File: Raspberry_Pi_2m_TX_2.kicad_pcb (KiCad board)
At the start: 2 copper layers, 66 x 56.5 mm, 32 parts, among them J3 RPi_GPIO, P1 3Sip100, P2 4Sip200, P3 2Sip200, P4 SMA, P5 CONN_01X02, Q1 BC817-40, U1 L4940V5 1.5A

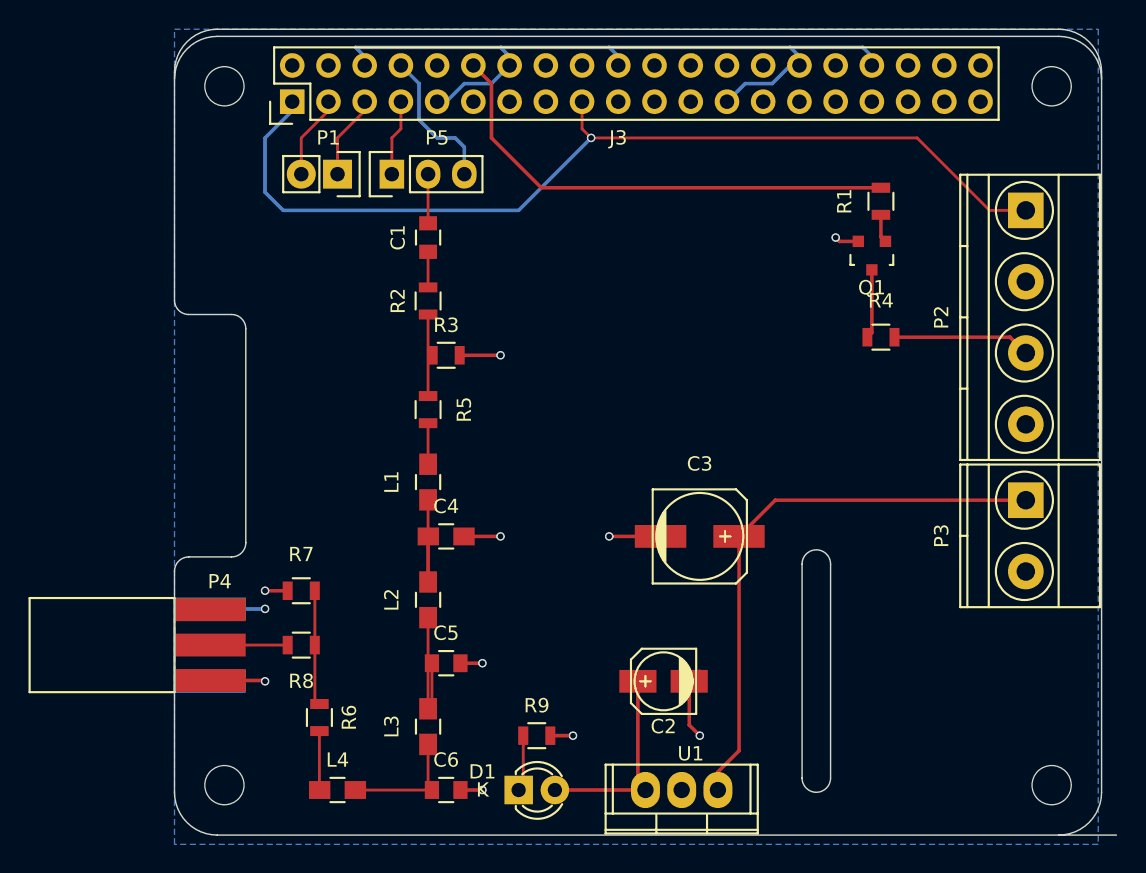
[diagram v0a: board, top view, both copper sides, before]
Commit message: Finished PCB but still need to do DRC
Almost complete
Still need to DRC and component check
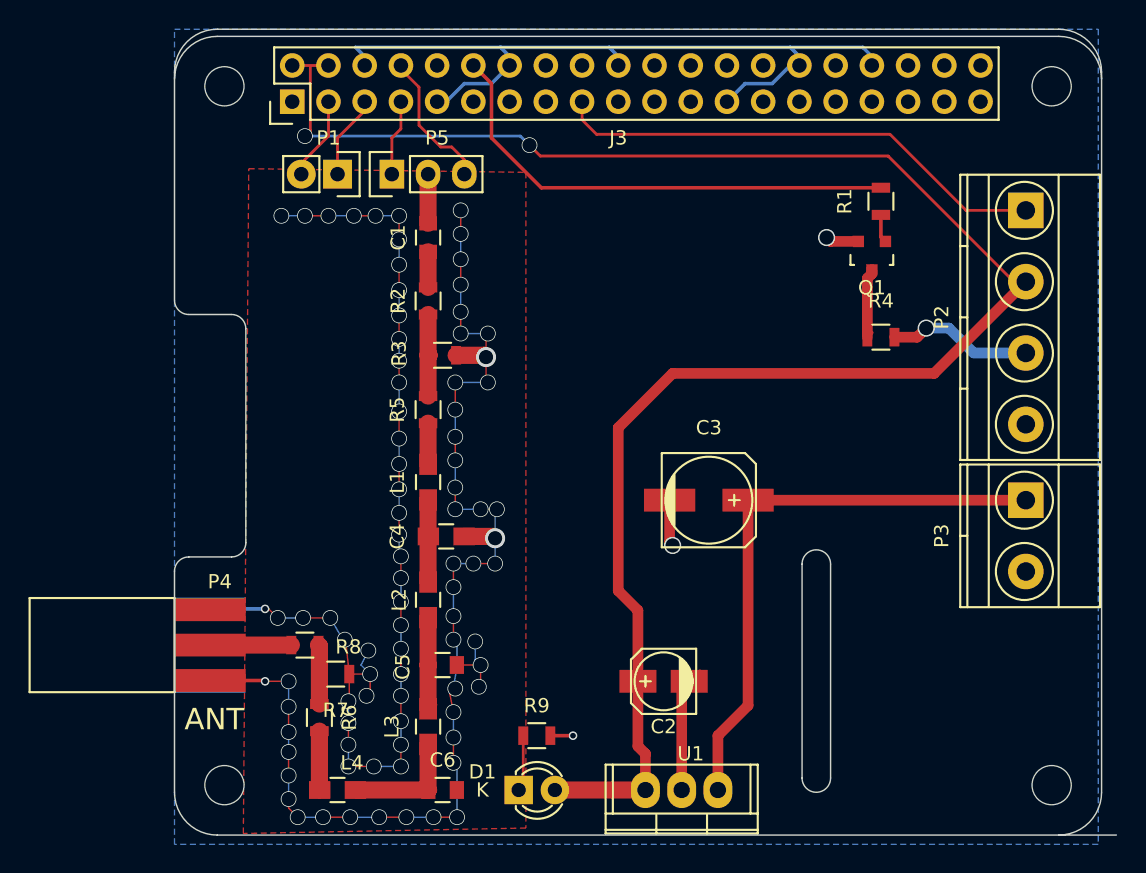
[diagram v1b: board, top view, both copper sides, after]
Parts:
- moved R7 6.32 mm to (46.9, 71.9), turned to 0 degrees
- moved C3 2.62 mm to (73.0, 59.7)
- moved C5 0.28 mm to (54.4, 71.2)
- moved C6 0.25 mm to (54.4, 80.0)
- moved R3 0.25 mm to (54.4, 49.5)
- moved R8 0.25 mm to (44.7, 69.8)
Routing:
- net GND: track 88.5 -> 239.1 mm, vias 11 -> 90
- net +5V: track 14.9 -> 129.2 mm, vias 0 -> 2
- net +3V3: track 68.0 -> 36.4 mm, vias 1 -> 0
- net Net-(R6-Pad1): track 8.07 -> 4.70 mm
- net Net-(C4-Pad1): track 8.96 -> 5.80 mm
- net Net-(C5-Pad1): track 9.70 -> 7.21 mm
- net Net-(C3-Pad1): track 39.6 -> 40.7 mm
- net Net-(J3-Pad3): track 5.87 -> 6.50 mm
- net Net-(P2-Pad3): track 9.67 -> 10.2 mm, vias 0 -> 1
- added copper zone on F.Cu, net GND
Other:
- net class +5V: trace_width 0.75 -> 1
- net class Default: trace_width 0.25 -> 1.2; via_dia 0.6 -> 1.1; via_drill 0.4 -> 1
- board text added: "ANT"

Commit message: Board is now compleate
Added second filter
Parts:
- added C7: 10nf, Capacitors_SMD:C_0805_HandSoldering, F.Cu at (48.8, 47.6)
- added F1: LFCN-80, Bacar:LFCN-80, F.Cu at (43.8, 40.6)
- added P6: CONN_01X02, Pin_Headers:Pin_Header_Straight_1x02, F.Cu at (48.8, 42.9)
- added P7: SMA, Bacar:SMA_Edge, F.Cu at (38.1, 40.8)
- added R10: oc, Resistors_SMD:R_0805_HandSoldering, F.Cu at (44.1, 50.5)
- added R11: 0, Resistors_SMD:R_0805_HandSoldering, F.Cu at (45.2, 45.7)
- added R12: 0, Resistors_SMD:R_0805_HandSoldering, F.Cu at (47.5, 53.8)
- moved D1 37.7 mm to (78.0, 47.0)
- moved R9 37.7 mm to (78.0, 42.5), turned to 90 degrees
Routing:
- net GND: track 239.1 -> 348.0 mm, vias 90 -> 138
- net +3V3: track 36.4 -> 57.9 mm
- net +5V: track 129.2 -> 109.5 mm
- net Net-(R10-Pad1): track 0.00 -> 7.17 mm
- net Net-(J3-Pad7): track 5.34 -> 11.3 mm
- net Net-(C7-Pad2): track 0.00 -> 5.01 mm
- net Net-(F1-Pad1): track 0.00 -> 3.67 mm
- net Net-(F1-Pad3): track 0.00 -> 3.59 mm
- net Net-(C7-Pad1): track 0.00 -> 3.45 mm
- net Net-(R6-Pad1): track 4.70 -> 6.84 mm
- net Net-(J3-Pad12): track 34.4 -> 33.7 mm
- net Net-(P2-Pad3): track 10.2 -> 9.67 mm, vias 1 -> 0
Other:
- net class Default: trace_width 1.2 -> 0.9; via_dia 1.1 -> 0.8; via_drill 1 -> 0.3
- board text added: "3V3"
- board text added: "5V"
- board text added: "ANT2"
- board text added: "GND"
- board text added: "PTT"
- board text added: "Rev 1.00 / 0217 SN_______________"
- board text added: "V6-9 +"
